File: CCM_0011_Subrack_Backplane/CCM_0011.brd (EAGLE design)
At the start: 406.4 x 101.6 mm, 23 parts, among them J1 PIN2F061.100, J2 PIN2F061.220, X1 FAB64S, X10 FAB64S, X11 FAB64S, X12 FAB64S, X13 FAB64S, X14 FAB64S, X15 FAB64S, X16 FAB64S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

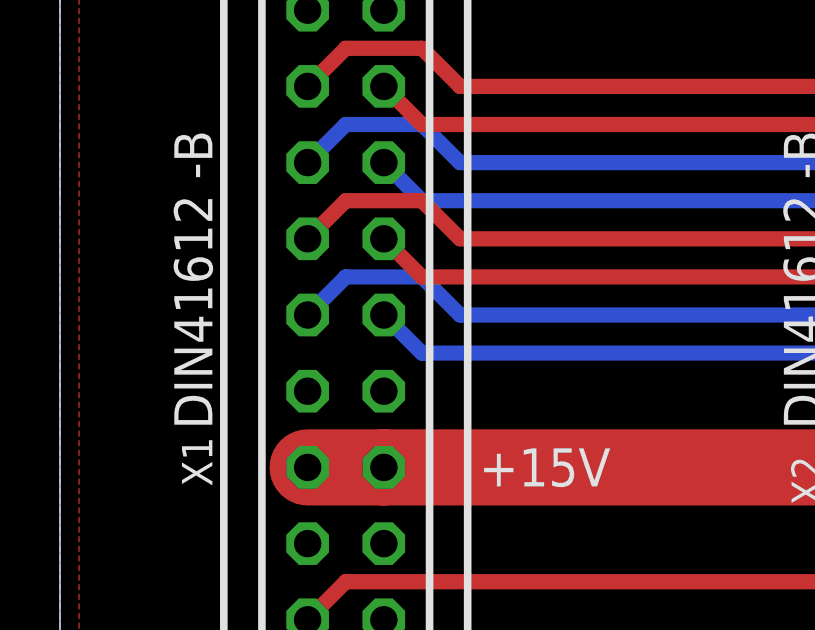
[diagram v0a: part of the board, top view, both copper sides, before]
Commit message: Shutter driver added.
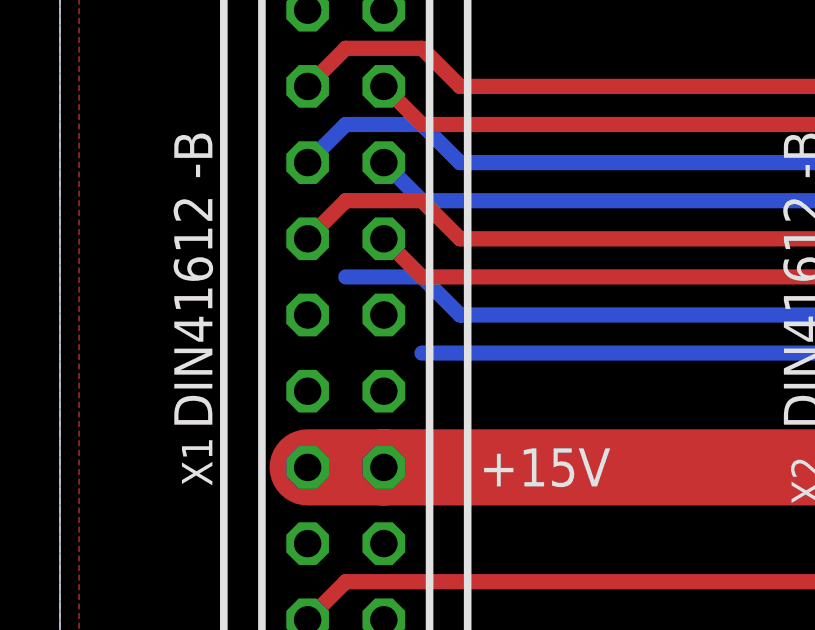
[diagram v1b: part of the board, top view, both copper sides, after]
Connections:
- new net MAINS_INDICATOR: X1.A15
- new net MAINS_SYNC: X1.B15
- net GPIO14: no longer X1.A15
- net GPIO15: no longer X1.B15
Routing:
- net GPIO14: track 406.1 -> 404.3 mm
- net GPIO15: track 406.1 -> 404.3 mm
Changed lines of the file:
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@@
 <?xml version="1.0" encoding="utf-8"?>
 <!DOCTYPE eagle SYSTEM "eagle.dtd">
-<eagle version="8.6.0">
+<eagle version="9.0.1">
 <drawing>
 <settings>
@@
 </signal>
 <signal name="GPIO14">
-<contactref element="X1" pad="A15"/>
 <contactref element="X2" pad="A15"/>
 <contactref element="X3" pad="A15"/>
@@
 <contactref element="X19" pad="A15"/>
 <contactref element="X20" pad="A15"/>
-<wire x1="8.255" y1="54.61" x2="9.525" y2="55.88" width="0.508" layer="16"/>
 <wire x1="9.525" y1="55.88" x2="12.065" y2="55.88" width="0.508" layer="16"/>
 <wire x1="12.065" y1="55.88" x2="13.335" y2="54.61" width="0.508" layer="16"/>
@@
 </signal>
 <signal name="GPIO15">
-<contactref element="X1" pad="B15"/>
 <contactref element="X2" pad="B15"/>
 <contactref element="X3" pad="B15"/>
@@
 <contactref element="X19" pad="B15"/>
 <contactref element="X20" pad="B15"/>
-<wire x1="10.795" y1="54.61" x2="12.065" y2="53.34" width="0.508" layer="16"/>
 <wire x1="12.065" y1="53.34" x2="29.845" y2="53.34" width="0.508" layer="16"/>
 <wire x1="29.845" y1="53.34" x2="31.115" y2="54.61" width="0.508" layer="16"/>
@@
 <wire x1="395.605" y1="78.74" x2="396.875" y2="80.01" width="0.508" layer="16"/>
 </signal>
+<signal name="MAINS_SYNC">
+<contactref element="X1" pad="B15"/>
+</signal>
+<signal name="MAINS_INDICATOR">
+<contactref element="X1" pad="A15"/>
+</signal>
 </signals>
